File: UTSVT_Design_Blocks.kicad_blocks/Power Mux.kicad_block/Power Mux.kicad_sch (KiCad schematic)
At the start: 8 parts, among them U1 TPS2117DRLR

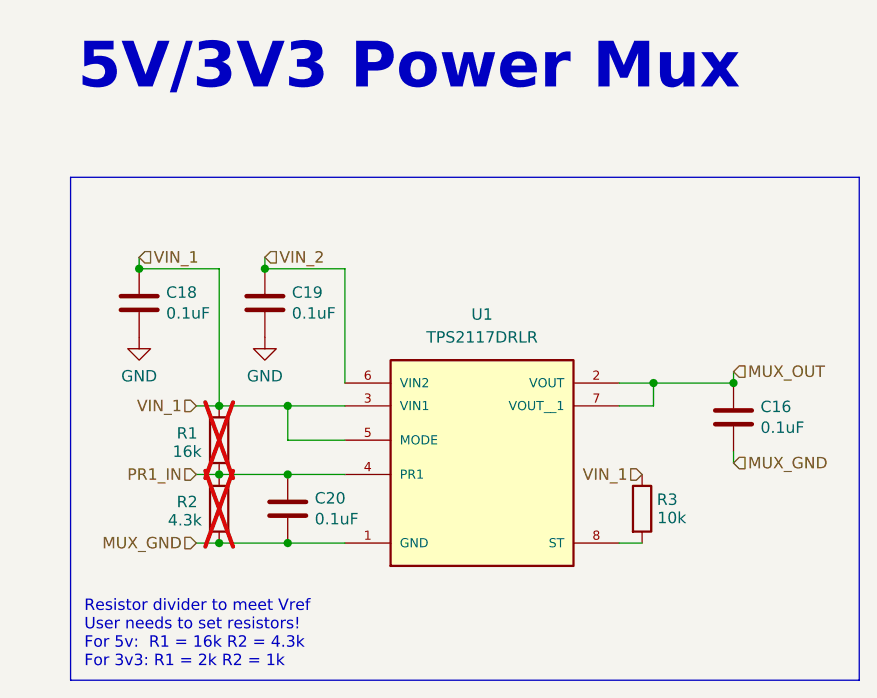
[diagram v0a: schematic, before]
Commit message: updated description for pwr mux
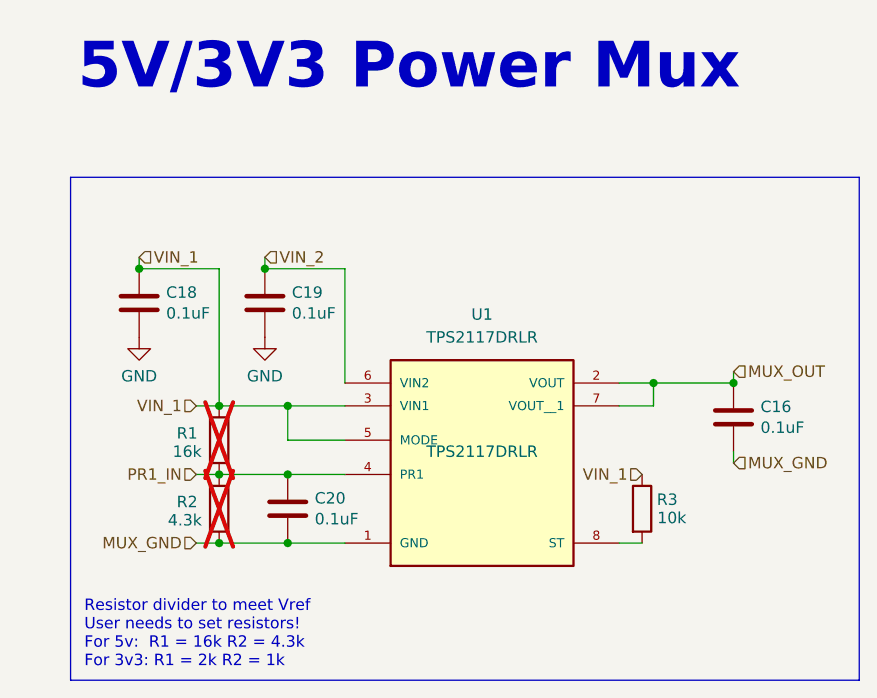
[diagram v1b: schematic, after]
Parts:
- U1: footprint TPS2117DRLR:SOTFL50P160X60-8N -> UTSVT_ICs:TPS2117DRLR; P/N (none) -> TPS2117DRLR
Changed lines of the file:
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@@
 			)
 		)
-		(property "Footprint" "TPS2117DRLR:SOTFL50P160X60-8N"
+		(property "Footprint" "UTSVT_ICs:TPS2117DRLR"
 			(at 71.12 68.58 0)
 			(effects
@@
 			)
 		)
+		(property "P/N" "TPS2117DRLR"
+			(at 71.12 68.58 0)
+			(effects
+				(font
+					(size 1.27 1.27)
+				)
+			)
+		)
